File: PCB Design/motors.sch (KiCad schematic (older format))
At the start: 9 parts, among them P3 CONN_01X03, P4 CONN_01X03, P5 CONN_01X03, P6 CONN_01X03, P7 CONN_01X03, P8 CONN_01X03, U2 LV8405V

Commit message: Added initial footprint associations, caps and resistors.
Kicad is giving weird errors for the libraries and BOM generator.
The libraries have to be downloaded manually from github, and
then added.

Signed-off-by: Kolijn Wolfaardt <kolijn.wolfaardt@gmail.com>
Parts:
- C10, C11: footprint (none) -> Capacitors_SMD:C_1206
- P3, P4, P5, P6, P7, P8: footprint (none) -> Pin_Headers:Pin_Header_Straight_1x03
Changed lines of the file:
@@
 F 0 "U2" H 5600 3200 60  0000 C CNN
 F 1 "LV8405V" H 5600 4200 60  0000 C CNN
-F 2 "" H 5800 3250 60  0000 C CNN
+F 2 "" H 5800 3250 60  0001 C CNN
 F 3 "" H 5800 3250 60  0000 C CNN
 	1    5600 3700
@@
 F 0 "P7" H 4950 1950 50  0000 C CNN
 F 1 "CONN_01X03" V 5050 1750 50  0000 C CNN
-F 2 "" H 4950 1750 60  0000 C CNN
+F 2 "Pin_Headers:Pin_Header_Straight_1x03" H 4950 1750 60  0001 C CNN
 F 3 "" H 4950 1750 60  0000 C CNN
 	1    4950 1750
@@
 F 0 "P8" H 6450 1950 50  0000 C CNN
 F 1 "CONN_01X03" V 6550 1750 50  0000 C CNN
-F 2 "" H 6450 1750 60  0000 C CNN
+F 2 "Pin_Headers:Pin_Header_Straight_1x03" H 6450 1750 60  0001 C CNN
 F 3 "" H 6450 1750 60  0000 C CNN
 	1    6450 1750
@@
 F 0 "P5" H 1700 4450 50  0000 C CNN
 F 1 "CONN_01X03" V 1800 4250 50  0000 C CNN
-F 2 "" H 1700 4250 60  0000 C CNN
+F 2 "Pin_Headers:Pin_Header_Straight_1x03" H 1700 4250 60  0001 C CNN
 F 3 "" H 1700 4250 60  0000 C CNN
 	1    1700 4250
@@
 F 0 "P4" H 1700 3500 50  0000 C CNN
 F 1 "CONN_01X03" V 1800 3300 50  0000 C CNN
-F 2 "" H 1700 3300 60  0000 C CNN
+F 2 "Pin_Headers:Pin_Header_Straight_1x03" H 1700 3300 60  0001 C CNN
 F 3 "" H 1700 3300 60  0000 C CNN
 	1    1700 3300
@@
 F 0 "C10" H 8250 3800 50  0000 L CNN
 F 1 "10nF" H 8250 3600 50  0000 L CNN
-F 2 "" H 8238 3550 30  0000 C CNN
+F 2 "Capacitors_SMD:C_1206" H 8238 3550 30  0001 C CNN
 F 3 "" H 8200 3700 60  0000 C CNN
 	1    8200 3700
@@
 F 0 "C11" H 9650 3750 50  0000 L CNN
 F 1 "100nF" H 9650 3550 50  0000 L CNN
-F 2 "" H 9638 3500 30  0000 C CNN
+F 2 "Capacitors_SMD:C_1206" H 9638 3500 30  0001 C CNN
 F 3 "" H 9600 3650 60  0000 C CNN
 	1    9600 3650
@@
 F 0 "P3" H 1650 5950 50  0000 C CNN
 F 1 "CONN_01X03" V 1750 5750 50  0000 C CNN
-F 2 "" H 1650 5750 60  0000 C CNN
+F 2 "Pin_Headers:Pin_Header_Straight_1x03" H 1650 5750 60  0001 C CNN
 F 3 "" H 1650 5750 60  0000 C CNN
 	1    1650 5750
@@
 F 0 "P6" H 3450 5900 50  0000 C CNN
 F 1 "CONN_01X03" V 3550 5700 50  0000 C CNN
-F 2 "" H 3450 5700 60  0000 C CNN
+F 2 "Pin_Headers:Pin_Header_Straight_1x03" H 3450 5700 60  0001 C CNN
 F 3 "" H 3450 5700 60  0000 C CNN
 	1    3450 5700

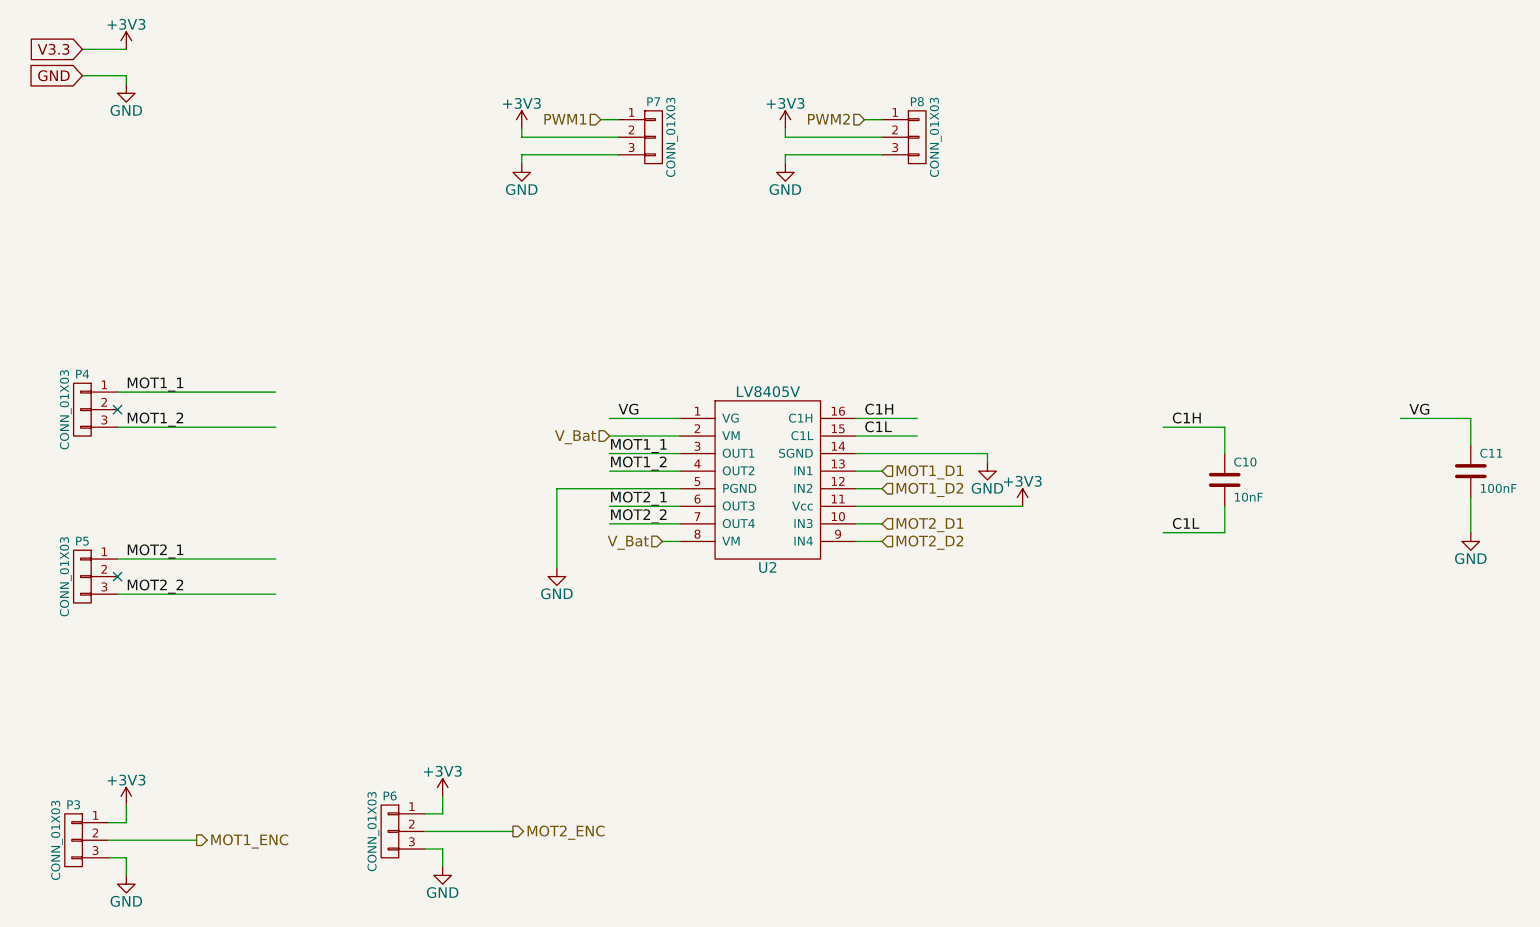
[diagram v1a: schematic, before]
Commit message: Added diodes to motor driver
Signed-off-by: Kolijn_Laptop <kolijn.wolfaardt@gmail.com>
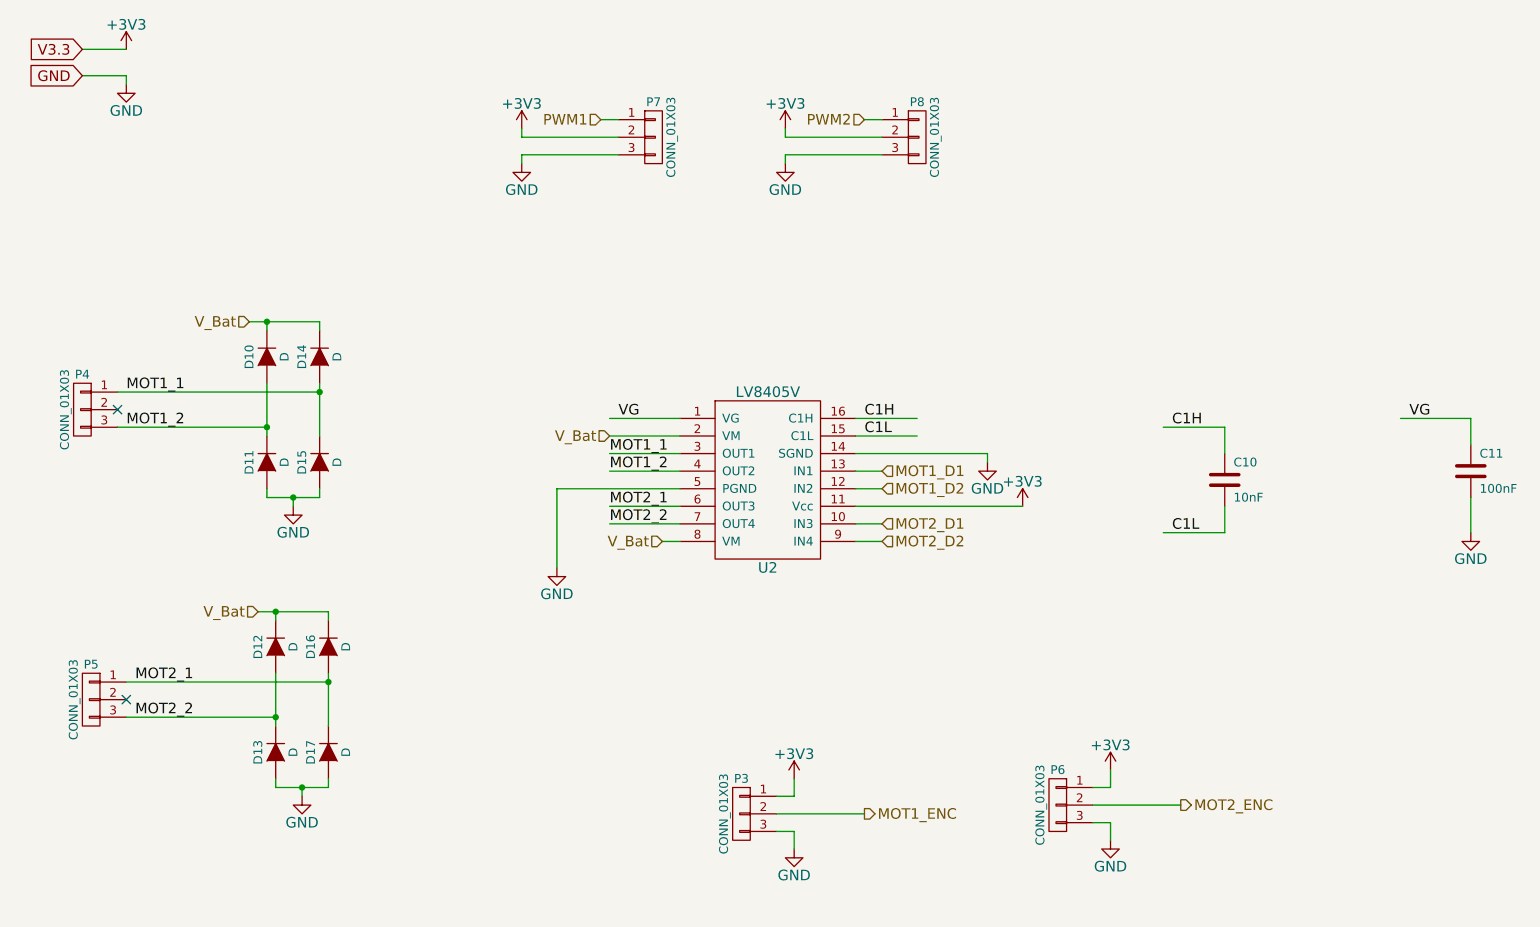
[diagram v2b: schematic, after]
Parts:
- added D10, D11, D12, D13, D14, D15, D16, D17: D, symbol D
- U2: footprint (none) -> Housings_SSOP:SSOP-16_4.4x5.2mm_Pitch0.65mm
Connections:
- wire segments 52 -> 70
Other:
- moved on the sheet: P3, P5, P6

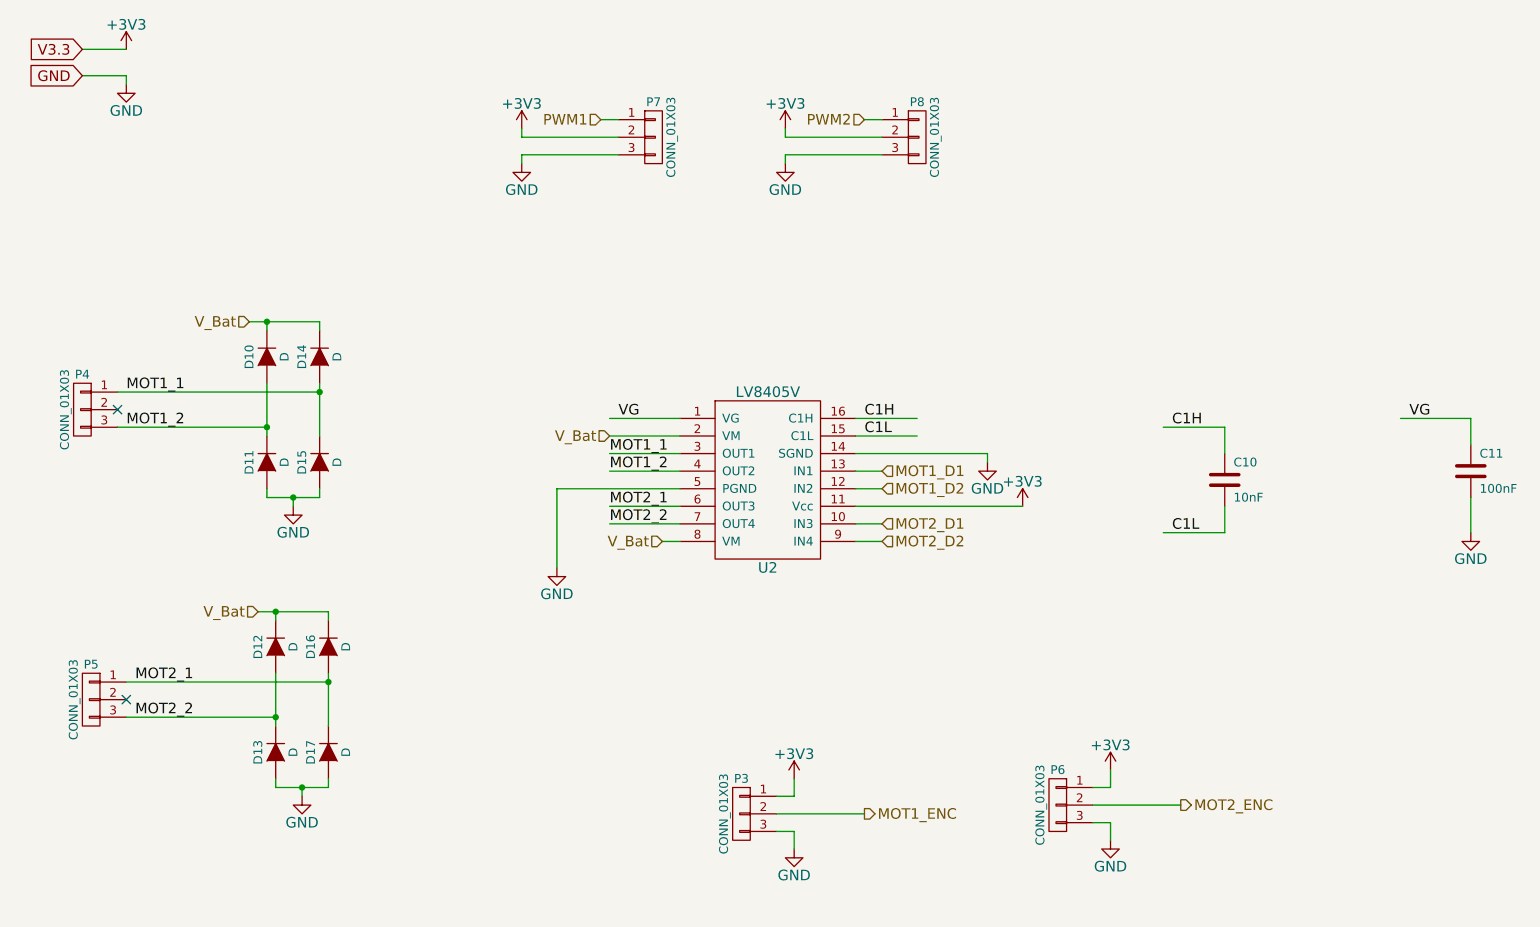
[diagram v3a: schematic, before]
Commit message: Finished the footprint allocation, started on the PCB layout.-s
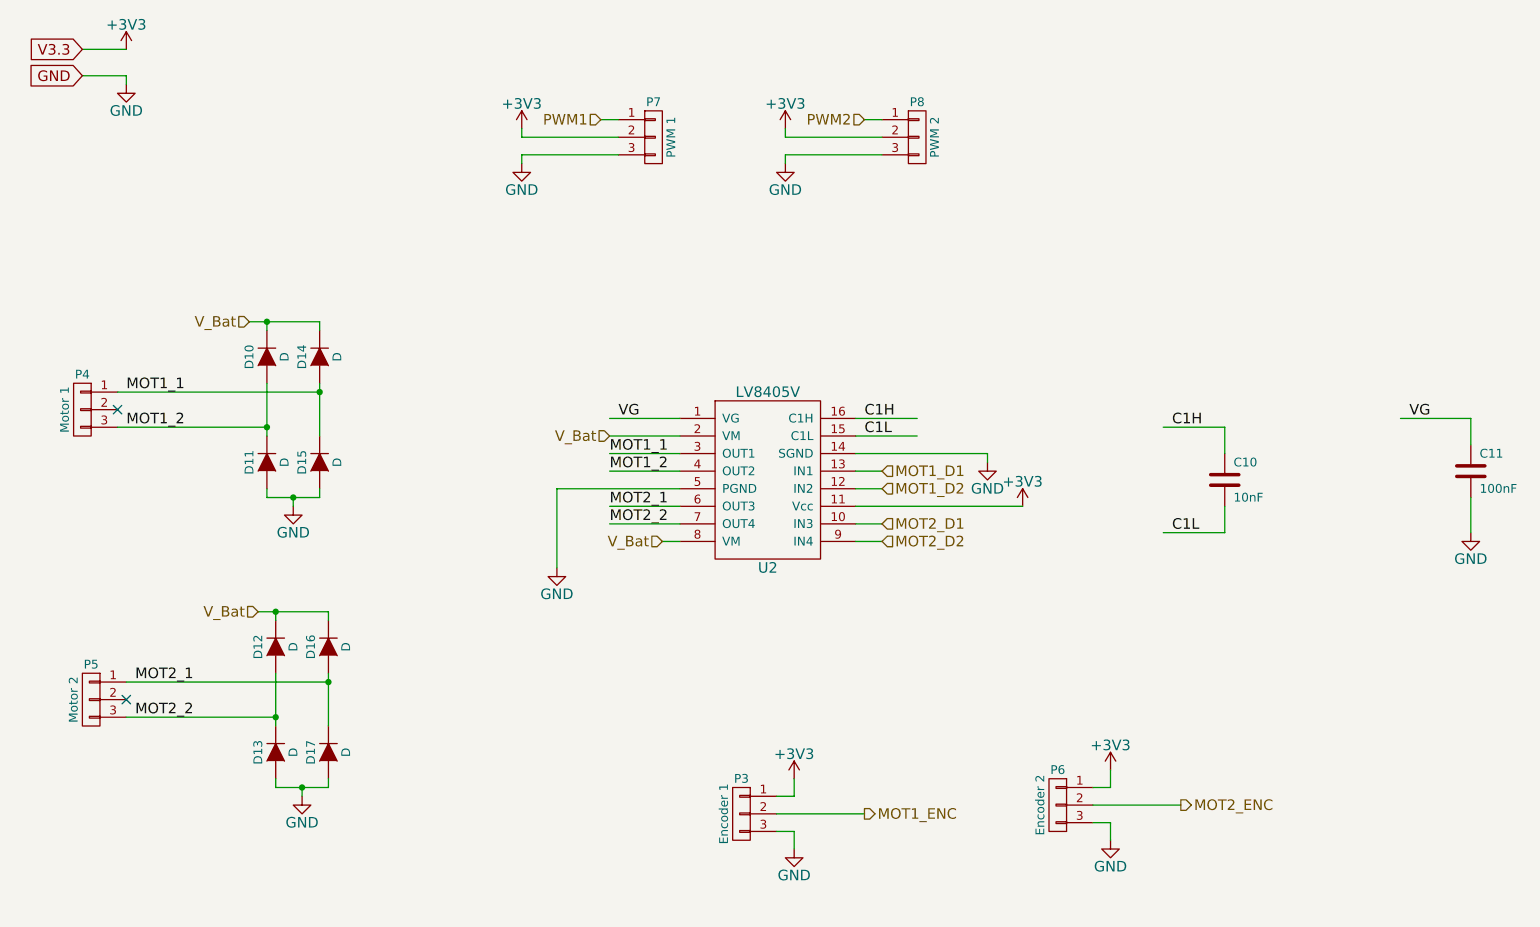
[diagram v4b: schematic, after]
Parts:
- D10, D11, D12, D13, D14, D15, D16, D17: footprint (none) -> Diodes_SMD:SOD-323
- P3: value CONN_01X03 -> Encoder 1
- P4: value CONN_01X03 -> Motor 1
- P5: value CONN_01X03 -> Motor 2
- P6: value CONN_01X03 -> Encoder 2
- P7: value CONN_01X03 -> PWM 1
- P8: value CONN_01X03 -> PWM 2
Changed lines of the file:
@@
 $EndComp
 $Comp
-L +3V3 #PWR9
+L +3V3 #PWR09
 U 1 1 5511E545
 P 1950 1250
-F 0 "#PWR9" H 1950 1100 60  0001 C CNN
+F 0 "#PWR09" H 1950 1100 60  0001 C CNN
 F 1 "+3V3" H 1950 1390 60  0000 C CNN
 F 2 "" H 1950 1250 60  0000 C CNN
@@
 $EndComp
 $Comp
-L GND #PWR10
+L GND #PWR010
 U 1 1 5511E54B
 P 1950 1450
-F 0 "#PWR10" H 1950 1200 60  0001 C CNN
+F 0 "#PWR010" H 1950 1200 60  0001 C CNN
 F 1 "GND" H 1950 1300 60  0000 C CNN
 F 2 "" H 1950 1450 60  0000 C CNN
@@
 P 4950 1750
 F 0 "P7" H 4950 1950 50  0000 C CNN
-F 1 "CONN_01X03" V 5050 1750 50  0000 C CNN
+F 1 "PWM 1" V 5050 1750 50  0000 C CNN
 F 2 "Pin_Headers:Pin_Header_Straight_1x03" H 4950 1750 60  0001 C CNN
 F 3 "" H 4950 1750 60  0000 C CNN
@@
 $EndComp
 $Comp
-L +3V3 #PWR13
+L +3V3 #PWR011
 U 1 1 5511E5F6
 P 4200 1700
-F 0 "#PWR13" H 4200 1550 60  0001 C CNN
+F 0 "#PWR011" H 4200 1550 60  0001 C CNN
 F 1 "+3V3" H 4200 1840 60  0000 C CNN
 F 2 "" H 4200 1700 60  0000 C CNN
@@
 $EndComp
 $Comp
-L GND #PWR14
+L GND #PWR012
 U 1 1 5511E627
 P 4200 1900
-F 0 "#PWR14" H 4200 1650 60  0001 C CNN
+F 0 "#PWR012" H 4200 1650 60  0001 C CNN
 F 1 "GND" H 4200 1750 60  0000 C CNN
 F 2 "" H 4200 1900 60  0000 C CNN
@@
 P 6450 1750
 F 0 "P8" H 6450 1950 50  0000 C CNN
-F 1 "CONN_01X03" V 6550 1750 50  0000 C CNN
+F 1 "PWM 2" V 6550 1750 50  0000 C CNN
 F 2 "Pin_Headers:Pin_Header_Straight_1x03" H 6450 1750 60  0001 C CNN
 F 3 "" H 6450 1750 60  0000 C CNN
@@
 $EndComp
 $Comp
-L +3V3 #PWR16
+L +3V3 #PWR013
 U 1 1 5511E6DC
 P 5700 1700
-F 0 "#PWR16" H 5700 1550 60  0001 C CNN
+F 0 "#PWR013" H 5700 1550 60  0001 C CNN
 F 1 "+3V3" H 5700 1840 60  0000 C CNN
 F 2 "" H 5700 1700 60  0000 C CNN
@@
 $EndComp
 $Comp
-L GND #PWR17
+L GND #PWR014
 U 1 1 5511E6E3
 P 5700 1900
-F 0 "#PWR17" H 5700 1650 60  0001 C CNN
+F 0 "#PWR014" H 5700 1650 60  0001 C CNN
 F 1 "GND" H 5700 1750 60  0000 C CNN
 F 2 "" H 5700 1900 60  0000 C CNN
@@
 P 1750 4950
 F 0 "P5" H 1750 5150 50  0000 C CNN
-F 1 "CONN_01X03" V 1850 4950 50  0000 C CNN
+F 1 "Motor 2" V 1850 4950 50  0000 C CNN
 F 2 "Pin_Headers:Pin_Header_Straight_1x03" H 1750 4950 60  0001 C CNN
 F 3 "" H 1750 4950 60  0000 C CNN
@@
 P 1700 3300
 F 0 "P4" H 1700 3500 50  0000 C CNN
-F 1 "CONN_01X03" V 1800 3300 50  0000 C CNN
+F 1 "Motor 1" V 1800 3300 50  0000 C CNN
 F 2 "Pin_Headers:Pin_Header_Straight_1x03" H 1700 3300 60  0001 C CNN
 F 3 "" H 1700 3300 60  0000 C CNN
@@
 $EndComp
 $Comp
-L GND #PWR20
+L GND #PWR015
 U 1 1 5511EBD6
 P 6850 3600
-F 0 "#PWR20" H 6850 3350 60  0001 C CNN
+F 0 "#PWR015" H 6850 3350 60  0001 C CNN
 F 1 "GND" H 6850 3450 60  0000 C CNN
 F 2 "" H 6850 3600 60  0000 C CNN
@@
 $EndComp
 $Comp
-L GND #PWR15
+L GND #PWR016
 U 1 1 5511EC3D
 P 4400 4200
-F 0 "#PWR15" H 4400 3950 60  0001 C CNN
+F 0 "#PWR016" H 4400 3950 60  0001 C CNN
 F 1 "GND" H 4400 4050 60  0000 C CNN
 F 2 "" H 4400 4200 60  0000 C CNN
@@
 $EndComp
 $Comp
-L +3V3 #PWR21
+L +3V3 #PWR017
 U 1 1 5511ECB8
 P 7050 3850
-F 0 "#PWR21" H 7050 3700 60  0001 C CNN
+F 0 "#PWR017" H 7050 3700 60  0001 C CNN
 F 1 "+3V3" H 7050 3990 60  0000 C CNN
 F 2 "" H 7050 3850 60  0000 C CNN
@@
 $EndComp
 $Comp
-L GND #PWR24
+L GND #PWR018
 U 1 1 5511F5A6
 P 9600 4000
-F 0 "#PWR24" H 9600 3750 60  0001 C CNN
+F 0 "#PWR018" H 9600 3750 60  0001 C CNN
 F 1 "GND" H 9600 3850 60  0000 C CNN
 F 2 "" H 9600 4000 60  0000 C CNN
@@
 P 5450 5600
 F 0 "P3" H 5450 5800 50  0000 C CNN
-F 1 "CONN_01X03" V 5550 5600 50  0000 C CNN
+F 1 "Encoder 1" V 5550 5600 50  0000 C CNN
 F 2 "Pin_Headers:Pin_Header_Straight_1x03" H 5450 5600 60  0001 C CNN
 F 3 "" H 5450 5600 60  0000 C CNN
@@
 $EndComp
 $Comp
-L GND #PWR19
+L GND #PWR019
 U 1 1 5511F8CF
 P 5750 5800
-F 0 "#PWR19" H 5750 5550 60  0001 C CNN
+F 0 "#PWR019" H 5750 5550 60  0001 C CNN
 F 1 "GND" H 5750 5650 60  0000 C CNN
 F 2 "" H 5750 5800 60  0000 C CNN
@@
 P 7250 5550
 F 0 "P6" H 7250 5750 50  0000 C CNN
-F 1 "CONN_01X03" V 7350 5550 50  0000 C CNN
+F 1 "Encoder 2" V 7350 5550 50  0000 C CNN
 F 2 "Pin_Headers:Pin_Header_Straight_1x03" H 7250 5550 60  0001 C CNN
 F 3 "" H 7250 5550 60  0000 C CNN
@@
 $EndComp
 $Comp
-L GND #PWR23
+L GND #PWR020
 U 1 1 5511FCDE
 P 7550 5750
-F 0 "#PWR23" H 7550 5500 60  0001 C CNN
+F 0 "#PWR020" H 7550 5500 60  0001 C CNN
 F 1 "GND" H 7550 5600 60  0000 C CNN
 F 2 "" H 7550 5750 60  0000 C CNN
@@
 NoConn ~ 1950 4950
 $Comp
-L +3V3 #PWR18
+L +3V3 #PWR021
 U 1 1 551360E1
 P 5750 5400
-F 0 "#PWR18" H 5750 5250 60  0001 C CNN
+F 0 "#PWR021" H 5750 5250 60  0001 C CNN
 F 1 "+3V3" H 5750 5540 60  0000 C CNN
 F 2 "" H 5750 5400 60  0000 C CNN
@@
 $EndComp
 $Comp
-L +3V3 #PWR22
+L +3V3 #PWR022
 U 1 1 55136185
 P 7550 5350
-F 0 "#PWR22" H 7550 5200 60  0001 C CNN
+F 0 "#PWR022" H 7550 5200 60  0001 C CNN
 F 1 "+3V3" H 7550 5490 60  0000 C CNN
 F 2 "" H 7550 5350 60  0000 C CNN
@@
 F 0 "D12" H 2800 4750 50  0000 C CNN
 F 1 "D" H 2800 4550 50  0000 C CNN
-F 2 "" H 2800 4650 60  0001 C CNN
+F 2 "Diodes_SMD:SOD-323" H 2800 4650 60  0001 C CNN
 F 3 "" H 2800 4650 60  0000 C CNN
 	1    2800 4650
@@
 F 0 "D16" H 3100 4750 50  0000 C CNN
 F 1 "D" H 3100 4550 50  0000 C CNN
-F 2 "" H 3100 4650 60  0001 C CNN
+F 2 "Diodes_SMD:SOD-323" H 3100 4650 60  0001 C CNN
 F 3 "" H 3100 4650 60  0000 C CNN
 	1    3100 4650
@@
 F 0 "D13" H 2800 5350 50  0000 C CNN
 F 1 "D" H 2800 5150 50  0000 C CNN
-F 2 "" H 2800 5250 60  0001 C CNN
+F 2 "Diodes_SMD:SOD-323" H 2800 5250 60  0001 C CNN
 F 3 "" H 2800 5250 60  0000 C CNN
 	1    2800 5250
@@
 F 0 "D17" H 3100 5350 50  0000 C CNN
 F 1 "D" H 3100 5150 50  0000 C CNN
-F 2 "" H 3100 5250 60  0001 C CNN
+F 2 "Diodes_SMD:SOD-323" H 3100 5250 60  0001 C CNN
 F 3 "" H 3100 5250 60  0000 C CNN
 	1    3100 5250
@@
 $EndComp
 $Comp
-L GND #PWR12
+L GND #PWR023
 U 1 1 551818E7
 P 2950 5500
-F 0 "#PWR12" H 2950 5250 60  0001 C CNN
+F 0 "#PWR023" H 2950 5250 60  0001 C CNN
 F 1 "GND" H 2950 5350 60  0000 C CNN
 F 2 "" H 2950 5500 60  0000 C CNN
@@
 F 0 "D10" H 2750 3100 50  0000 C CNN
 F 1 "D" H 2750 2900 50  0000 C CNN
-F 2 "" H 2750 3000 60  0001 C CNN
+F 2 "Diodes_SMD:SOD-323" H 2750 3000 60  0001 C CNN
 F 3 "" H 2750 3000 60  0000 C CNN
 	1    2750 3000
@@
 F 0 "D14" H 3050 3100 50  0000 C CNN
 F 1 "D" H 3050 2900 50  0000 C CNN
-F 2 "" H 3050 3000 60  0001 C CNN
+F 2 "Diodes_SMD:SOD-323" H 3050 3000 60  0001 C CNN
 F 3 "" H 3050 3000 60  0000 C CNN
 	1    3050 3000
@@
 F 0 "D11" H 2750 3700 50  0000 C CNN
 F 1 "D" H 2750 3500 50  0000 C CNN
-F 2 "" H 2750 3600 60  0001 C CNN
+F 2 "Diodes_SMD:SOD-323" H 2750 3600 60  0001 C CNN
 F 3 "" H 2750 3600 60  0000 C CNN
 	1    2750 3600
@@
 F 0 "D15" H 3050 3700 50  0000 C CNN
 F 1 "D" H 3050 3500 50  0000 C CNN
-F 2 "" H 3050 3600 60  0001 C CNN
+F 2 "Diodes_SMD:SOD-323" H 3050 3600 60  0001 C CNN
 F 3 "" H 3050 3600 60  0000 C CNN
 	1    3050 3600
@@
 $EndComp
 $Comp
-L GND #PWR11
+L GND #PWR024
 U 1 1 55182151
 P 2900 3850
-F 0 "#PWR11" H 2900 3600 60  0001 C CNN
+F 0 "#PWR024" H 2900 3600 60  0001 C CNN
 F 1 "GND" H 2900 3700 60  0000 C CNN
 F 2 "" H 2900 3850 60  0000 C CNN
